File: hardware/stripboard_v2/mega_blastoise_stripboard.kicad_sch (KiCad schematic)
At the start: 26 parts, among them J1 ST7796 3.5in 320x480 SPI, J2 TP4056 B+ B-, J3 TP4056 OUT+ OUT-, SW1 P1_UP, SW10 P2_DOWN, SW11 P2_LEFT, SW12 P2_RIGHT, SW13 P2_A, SW14 P2_B, SW15 P2_INFO, SW16 P2_MENU, SW17 Power slide switch, SW2 P1_DOWN, SW3 P1_LEFT, SW4 P1_RIGHT, SW5 P1_A, SW6 P1_B, SW7 P1_INFO, SW8 P1_MENU, SW9 P2_UP, U1 Pico 2 (RP2350)

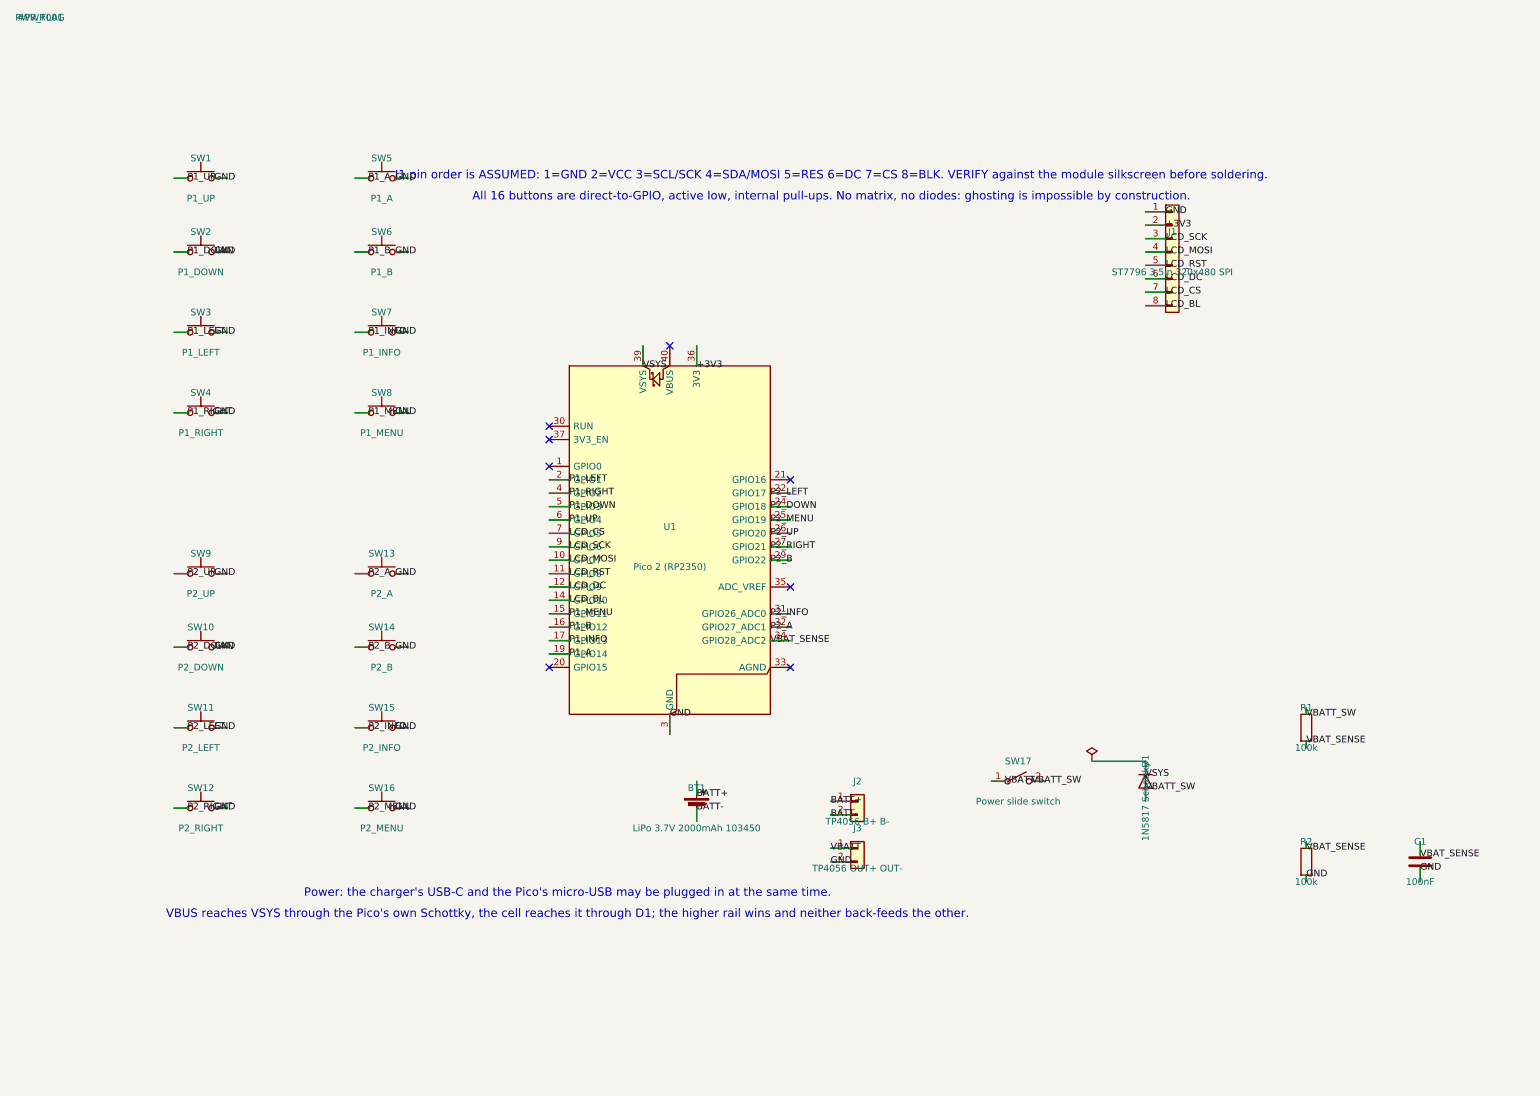
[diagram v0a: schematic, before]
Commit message: Point every net label away from the part it belongs to
The generator that drew this sheet ran each pin stub inward, so all 82 net
labels were printed across their own symbol, and nine parts had Reference
and Value parked exactly on a pin endpoint. Reading the power section meant
picking VBATT_SW out of the middle of a resistor.

The stubs now run outward from the pin, using the library's own pin angle to
decide which way that is, and each label takes the rotation and justification
that makes its text read away from the body. Fields that sat on terminals move
beside them instead, and the sheet notes are re-flowed into the empty column
next to the Pico rather than running off the page edge.

A few parts move: R1 up, R2 and C1 up off the title block, SW17 left of D1's
designator. The netlist is unchanged, pin for pin, and check_text_overlap.py
now reports zero colliding text boxes.

Co-Authored-By: Claude Opus 5 <noreply@anthropic.com>
Claude-Session: https://claude.ai/code/session_01DtJPckCX3BS4baXMVDqKJx
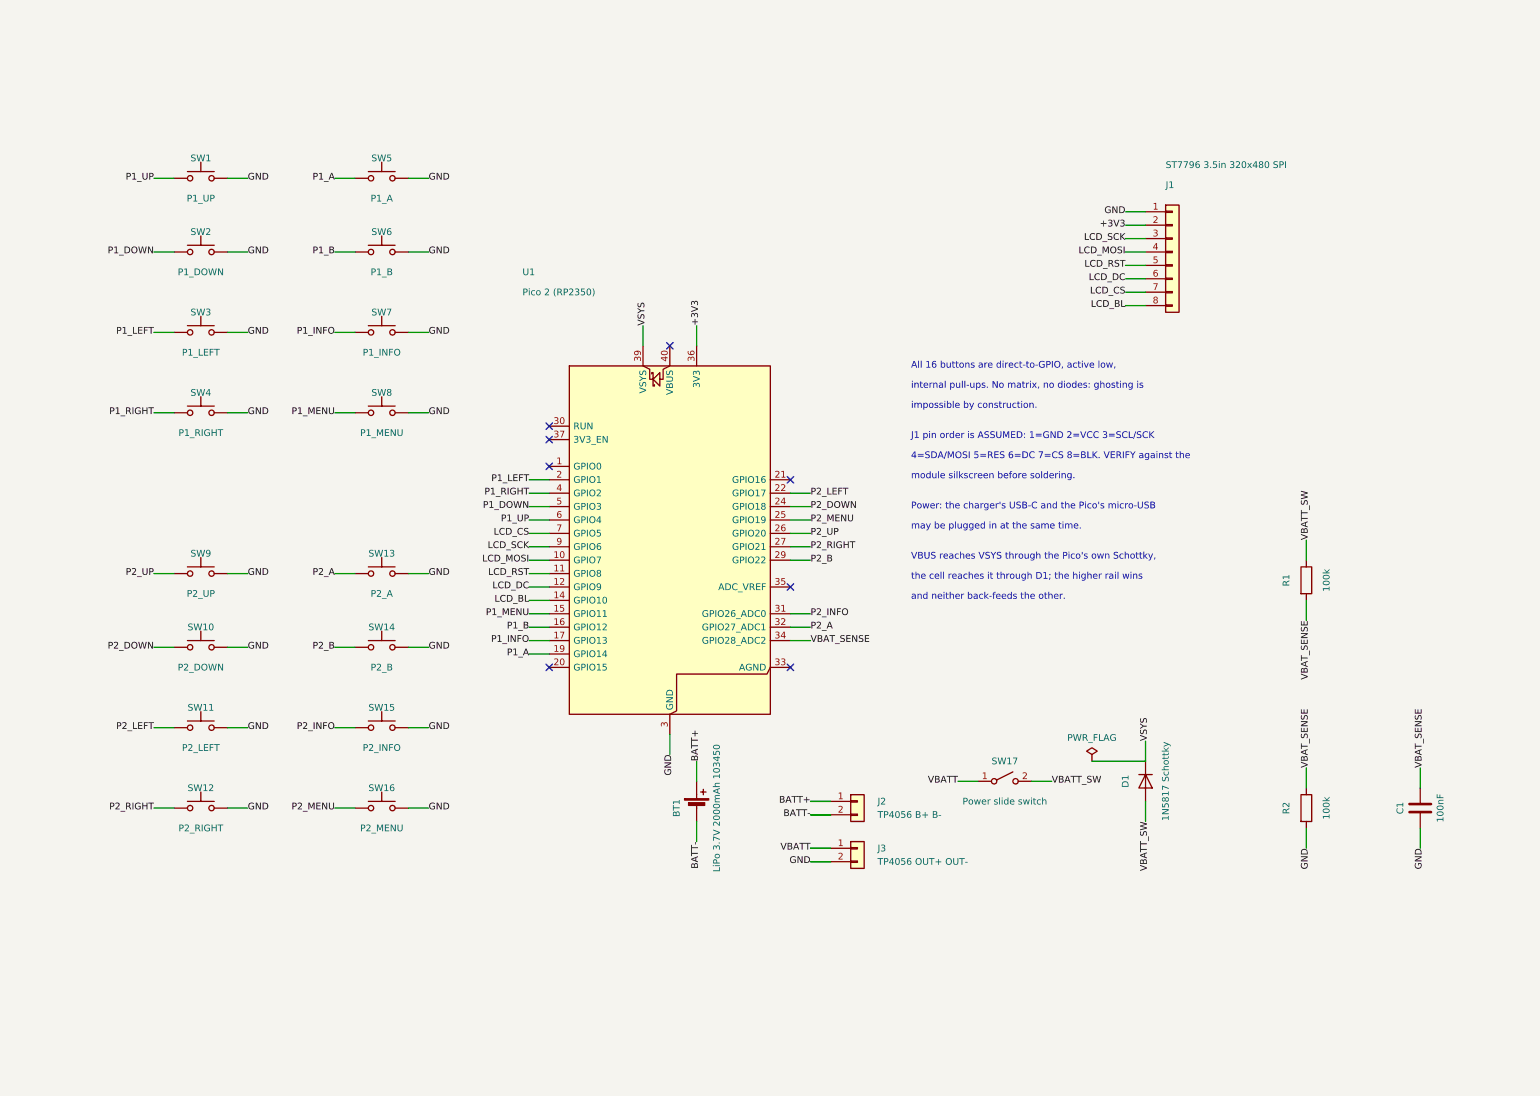
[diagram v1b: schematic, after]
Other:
- note added: "4=SDA/MOSI 5=RES 6=DC 7=CS 8=BLK. VERIFY against the"
- note added: "All 16 buttons are direct-to-GPIO, active low,"
- note added: "J1 pin order is ASSUMED: 1=GND 2=VCC 3=SCL/SCK"
- note added: "Power: the charger's USB-C and the Pico's micro-USB"
- note added: "VBUS reaches VSYS through the Pico's own Schottky,"
- note added: "and neither back-feeds the other."
- note added: "impossible by construction."
- note added: "internal pull-ups. No matrix, no diodes: ghosting is"
- note added: "may be plugged in at the same time."
- note added: "module silkscreen before soldering."
- note added: "the cell reaches it through D1; the higher rail wins"
- note removed: "All 16 buttons are direct-to-GPIO, active low, internal pull-ups. No matrix, no diodes: ghosting is impossible by construction."
- note removed: "J1 pin order is ASSUMED: 1=GND 2=VCC 3=SCL/SCK 4=SDA/MOSI 5=RES 6=DC 7=CS 8=BLK. VERIFY against the module silkscreen before soldering."
- note removed: "Power: the charger's USB-C and the Pico's micro-USB may be plugged in at the same time."
- note removed: "VBUS reaches VSYS through the Pico's own Schottky, the cell reaches it through D1; the higher rail wins and neither back-feeds the other."
- moved on the sheet: C1, R1, R2, SW17

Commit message: Draw the power train as a chain instead of nine strangers
Every net on the sheet was joined by name. For the button banks that is right:
each switch really is an island. For the power train it hid the only thing that
matters about it, which is that the cell reaches VSYS through a path you should
be able to follow with a finger.

The nine parts now sit left to right in the order the current takes: cell into
the charger's B+/B-, protected output out through the slide switch, through D1,
out to VSYS. The sense divider hangs off the switched rail ahead of the diode,
where it actually taps. One ground rail runs along the foot. A dashed box says
where the module stops, and the two nets that leave it cross that boundary.

Net names all survive; each keeps a single label, now sitting on the wire that
carries it rather than hung off a pin. The netlist is identical to the original
schematic, pin for pin, 38 nets.

D1 is mirrored rather than rotated 180, because rotating it takes its reference
and value upside down with it.

The notes move to the band under the button banks, which is where there is now
room, since the column they were in is where the module lives.

Co-Authored-By: Claude Opus 5 <noreply@anthropic.com>
Claude-Session: https://claude.ai/code/session_01DtJPckCX3BS4baXMVDqKJx
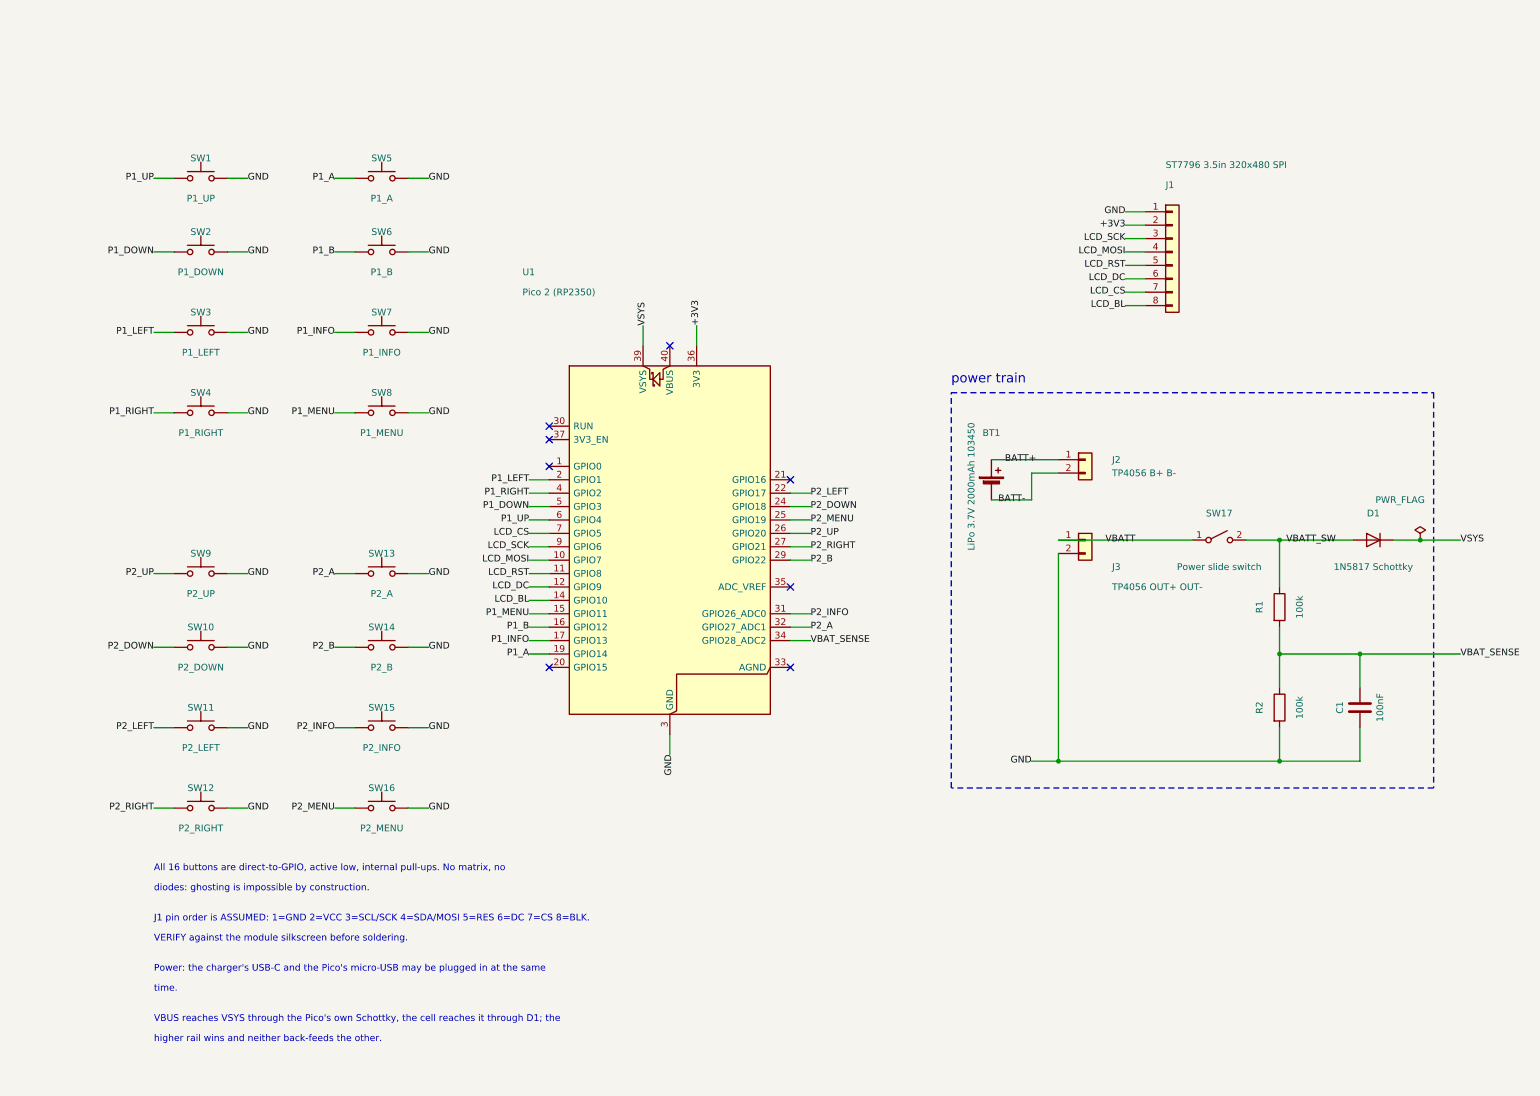
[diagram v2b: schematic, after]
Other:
- note added: "All 16 buttons are direct-to-GPIO, active low, internal pull-ups. No matrix, no"
- note added: "J1 pin order is ASSUMED: 1=GND 2=VCC 3=SCL/SCK 4=SDA/MOSI 5=RES 6=DC 7=CS 8=BLK."
- note added: "Power: the charger's USB-C and the Pico's micro-USB may be plugged in at the same"
- note added: "VBUS reaches VSYS through the Pico's own Schottky, the cell reaches it through D1; the"
- note added: "VERIFY against the module silkscreen before soldering."
- note added: "diodes: ghosting is impossible by construction."
- note added: "higher rail wins and neither back-feeds the other."
- note added: "power train"
- note added: "time."
- note removed: "4=SDA/MOSI 5=RES 6=DC 7=CS 8=BLK. VERIFY against the"
- note removed: "All 16 buttons are direct-to-GPIO, active low,"
- note removed: "J1 pin order is ASSUMED: 1=GND 2=VCC 3=SCL/SCK"
- note removed: "Power: the charger's USB-C and the Pico's micro-USB"
- note removed: "VBUS reaches VSYS through the Pico's own Schottky,"
- note removed: "and neither back-feeds the other."
- note removed: "impossible by construction."
- note removed: "internal pull-ups. No matrix, no diodes: ghosting is"
- note removed: "may be plugged in at the same time."
- note removed: "module silkscreen before soldering."
- note removed: "the cell reaches it through D1; the higher rail wins"
- moved on the sheet: BT1, C1, D1, J2, J3, R1, R2, SW17

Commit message: The real display module is pin-reversed; reroute for it
Alex laid the module on the board with every landmark checked and GND arrived
at the charger edge, not the Pico edge: this module's header reads BL..GND
where the design assumed GND..BL. Rather than fight it, the socket stays put
and the roles move.

Five signals still fall straight through to the GPIO under their column, just
different ones: BL to GP5, DC to GP6, RST to GP7, MOSI to GP8, SCK to GP9. CS
takes the orphaned GP10 through the one new signal wire. The power pins swap
ends of the socket: VCC keeps its wire from 3V3 at the other end, and GND gets
its column split off GP10 and bridged onto the P1 bus.

Physical delta from the old plan, for a board already partly cut: do not cut
I45 (bridge it if cut), add cuts I48 and P42, move two wires, add one 5 mm
ground bridge. Everything else stands.

The price is hardware SPI: SCK over GP9 and MOSI over GP8 is a pair no SPI
block can drive, so the firmware clocks the panel by PIO. BUILD.md says so
where it used to argue for SPI0.

Schematic, netlist (exactly the eight display nets moved), cut guide, paper
template, marking stencil, PSD and solid models all regenerated from the one
source. verify.py passes: 30 nets, 44 cuts, 16 wires, 356 mm.

Co-Authored-By: Claude Opus 5 <noreply@anthropic.com>
Claude-Session: https://claude.ai/code/session_01DtJPckCX3BS4baXMVDqKJx
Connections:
- net +3V3: now also J1.7 (Pin_7); no longer J1.2 (Pin_2)
- net GND: now also J1.8 (Pin_8); no longer J1.1 (Pin_1)
- net LCD_BL: now also J1.1 (Pin_1), U1.7 (GPIO5); no longer J1.8 (Pin_8), U1.14 (GPIO10)
- net LCD_CS: now also J1.2 (Pin_2), U1.14 (GPIO10); no longer J1.7 (Pin_7), U1.7 (GPIO5)
- net LCD_DC: now also J1.3 (Pin_3), U1.9 (GPIO6); no longer J1.6 (Pin_6), U1.12 (GPIO9)
- net LCD_MOSI: now also J1.5 (Pin_5), U1.11 (GPIO8); no longer J1.4 (Pin_4), U1.10 (GPIO7)
- net LCD_RST: now also J1.4 (Pin_4), U1.10 (GPIO7); no longer J1.5 (Pin_5), U1.11 (GPIO8)
- net LCD_SCK: now also J1.6 (Pin_6), U1.12 (GPIO9); no longer J1.3 (Pin_3), U1.9 (GPIO6)
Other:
- note added: "GND. SCK/MOSI land on GP9/GP8, so the firmware drives the panel by PIO, not hardware"
- note added: "J1 pin order is VERIFIED against the real module, which is REVERSED from the usual"
- note added: "SPI."
- note added: "ST7796 boards: socket position 1 receives module pin 8 (BL) and position 8 receives"
- note removed: "J1 pin order is ASSUMED: 1=GND 2=VCC 3=SCL/SCK 4=SDA/MOSI 5=RES 6=DC 7=CS 8=BLK."
- note removed: "VERIFY against the module silkscreen before soldering."
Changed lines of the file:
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@@
 		)
 	)
-	(label "LCD_DC"
+	(label "LCD_SCK"
 		(at 92.71 107.95 180)
 		(effects
@@
 		)
 	)
-	(label "LCD_RST"
+	(label "LCD_MOSI"
 		(at 92.71 105.41 180)
 		(effects
@@
 		)
 	)
-	(label "LCD_BL"
+	(label "LCD_CS"
 		(at 92.71 110.49 180)
 		(effects
@@
 		)
 	)
-	(label "+3V3"
+	(label "LCD_CS"
 		(at 205.74 39.37 180)
 		(effects
@@
 		)
 	)
-	(label "GND"
+	(label "LCD_BL"
 		(at 205.74 36.83 180)
 		(effects
@@
 		)
 	)
-	(label "LCD_CS"
+	(label "LCD_BL"
 		(at 92.71 97.79 180)
 		(effects
@@
 		)
 	)
-	(label "LCD_SCK"
+	(label "LCD_DC"
 		(at 92.71 100.33 180)
 		(effects
@@
 		)
 	)
-	(label "LCD_MOSI"
+	(label "LCD_RST"
 		(at 92.71 102.87 180)
 		(effects
@@
 		)
 	)
-	(label "LCD_DC"
+	(label "LCD_SCK"
 		(at 205.74 49.53 180)
 		(effects
@@
 		)
 	)
-	(label "LCD_RST"
+	(label "LCD_MOSI"
 		(at 205.74 46.99 180)
 		(effects
@@
 		)
 	)
-	(label "LCD_BL"
+	(label "GND"
 		(at 205.74 54.61 180)
 		(effects
@@
 		)
 	)
-	(label "LCD_SCK"
+	(label "LCD_DC"
 		(at 205.74 41.91 180)
 		(effects
@@
 		)
 	)
-	(label "LCD_MOSI"
+	(label "LCD_RST"
 		(at 205.74 44.45 180)
 		(effects
@@
 		)
 	)
-	(label "LCD_CS"
+	(label "+3V3"
 		(at 205.74 52.07 180)
 		(effects
@@
 	(wire
 		(pts
+			(xy 187.96 91.44)
+			(xy 187.96 86.36)
+		)
+		(stroke
+			(width 0)
+			(type default)
+		)
+		(uuid "pwr-w2")
+	)
+	(wire
+		(pts
+			(xy 234.95 120.65)
+			(xy 250.19 120.65)
+		)
+		(stroke
+			(width 0)
+			(type default)
+		)
+		(uuid "pwr-w11")
+	)
+	(wire
+		(pts
+			(xy 250.19 120.65)
+			(xy 269.24 120.65)
+		)
+		(stroke
+			(width 0)
+			(type default)
+		)
+		(uuid "pwr-w13")
+	)
+	(wire
+		(pts
+			(xy 187.96 140.97)
+			(xy 250.19 140.97)
+		)
+		(stroke
+			(width 0)
+			(type default)
+		)
+		(uuid "pwr-w15")
+	)
+	(wire
+		(pts
+			(xy 187.96 91.44)
+			(xy 187.96 86.36)
+		)
+		(stroke
+			(width 0)
+			(type default)
+		)
+		(uuid "pwr-w2")
+	)
+	(wire
+		(pts
+			(xy 234.95 120.65)
+			(xy 250.19 120.65)
+		)
+		(stroke
+			(width 0)
+			(type default)
+		)
+		(uuid "pwr-w11")
+	)
+	(wire
+		(pts
+			(xy 250.19 120.65)
+			(xy 269.24 120.65)
+		)
+		(stroke
+			(width 0)
+			(type default)
+		)
+		(uuid "pwr-w13")
+	)
+	(wire
+		(pts
+			(xy 187.96 140.97)
+			(xy 250.19 140.97)
+		)
+		(stroke
+			(width 0)
+			(type default)
+		)
+		(uuid "pwr-w15")
+	)
+	(wire
+		(pts
 			(xy 180.34 83.82)
 			(xy 193.04 83.82)
@@
 		(uuid "pwr-note0-165_1")
 	)
-	(text "J1 pin order is ASSUMED: 1=GND 2=VCC 3=SCL/SCK 4=SDA/MOSI 5=RES 6=DC 7=CS 8=BLK."
+	(text "J1 pin order is VERIFIED against the real module, which is REVERSED from the usual"
 		(at 21.59 170.815 0)
 		(effects
@@
 		(uuid "pwr-note1-170_815")
 	)
-	(text "VERIFY against the module silkscreen before soldering."
+	(text "ST7796 boards: socket position 1 receives module pin 8 (BL) and position 8 receives"
 		(at 21.59 174.625 0)
 		(effects
@@
 		(uuid "pwr-note1-174_625")
 	)
+	(text "GND. SCK/MOSI land on GP9/GP8, so the firmware drives the panel by PIO, not hardware"
+		(at 21.59 178.435 0)
+		(effects
+			(font
+				(size 1.27 1.27)
+			)
+			(justify left)
+		)
+		(uuid "pwr-note1-178_435")
+	)
+	(text "SPI."
+		(at 21.59 182.245 0)
+		(effects
+			(font
+				(size 1.27 1.27)
+			)
+			(justify left)
+		)
+		(uuid "pwr-note1-182_245")
+	)
 	(text "Power: the charger's USB-C and the Pico's micro-USB may be plugged in at the same"
-		(at 21.59 180.34 0)
-		(effects
-			(font
-				(size 1.27 1.27)
-			)
-			(justify left)
-		)
-		(uuid "pwr-note2-180_34")
+		(at 21.59 187.96 0)
+		(effects
+			(font
+				(size 1.27 1.27)
+			)
+			(justify left)
+		)
+		(uuid "pwr-note2-187_96")
 	)
 	(text "time."
-		(at 21.59 184.15 0)
-		(effects
-			(font
-				(size 1.27 1.27)
-			)
-			(justify left)
-		)
-		(uuid "pwr-note2-184_15")
+		(at 21.59 191.77 0)
+		(effects
+			(font
+				(size 1.27 1.27)
+			)
+			(justify left)
+		)
+		(uuid "pwr-note2-191_77")
 	)
 	(text "VBUS reaches VSYS through the Pico's own Schottky, the cell reaches it through D1; the"
-		(at 21.59 189.865 0)
-		(effects
-			(font
-				(size 1.27 1.27)
-			)
-			(justify left)
-		)
-		(uuid "pwr-note3-189_865")
+		(at 21.59 197.485 0)
+		(effects
+			(font
+				(size 1.27 1.27)
+			)
+			(justify left)
+		)
+		(uuid "pwr-note3-197_485")
 	)
 	(text "higher rail wins and neither back-feeds the other."
-		(at 21.59 193.675 0)
-		(effects
-			(font
-				(size 1.27 1.27)
-			)
-			(justify left)
-		)
-		(uuid "pwr-note3-193_675")
+		(at 21.59 201.295 0)
+		(effects
+			(font
+				(size 1.27 1.27)
+			)
+			(justify left)
+		)
+		(uuid "pwr-note3-201_295")
 	)
 )
